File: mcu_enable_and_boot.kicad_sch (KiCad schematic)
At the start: 12 parts, among them SW1 TS_Basic_Small, SW2 TS_Basic_Small

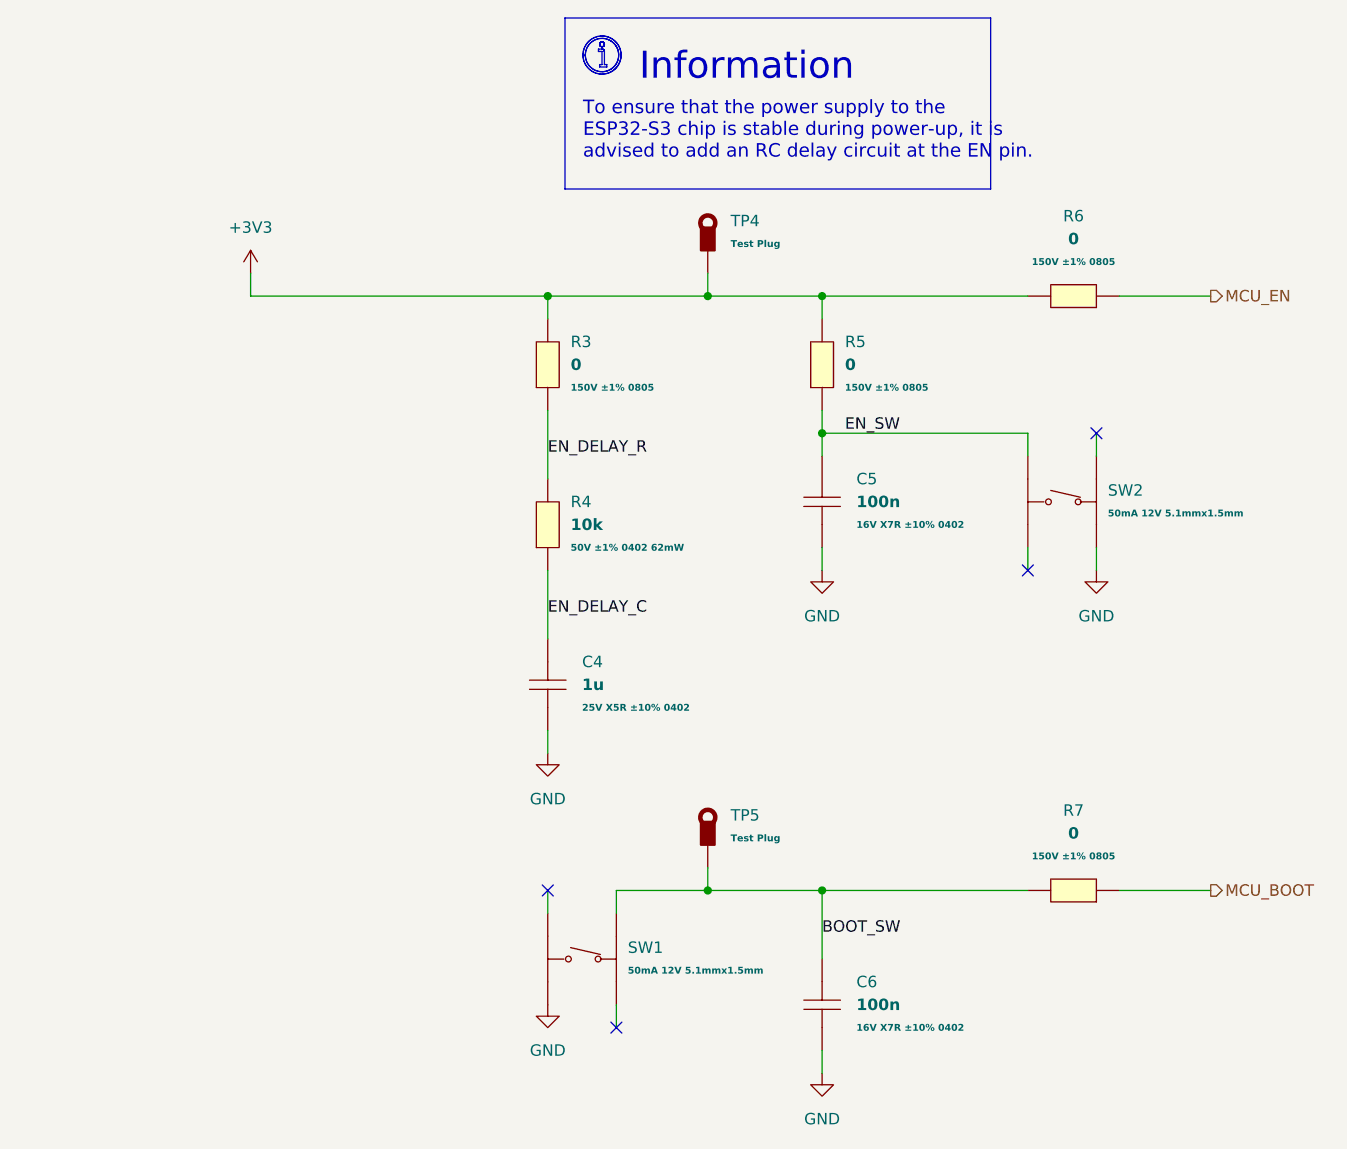
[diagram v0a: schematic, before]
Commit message: Updated library name, updated and verified all footprints
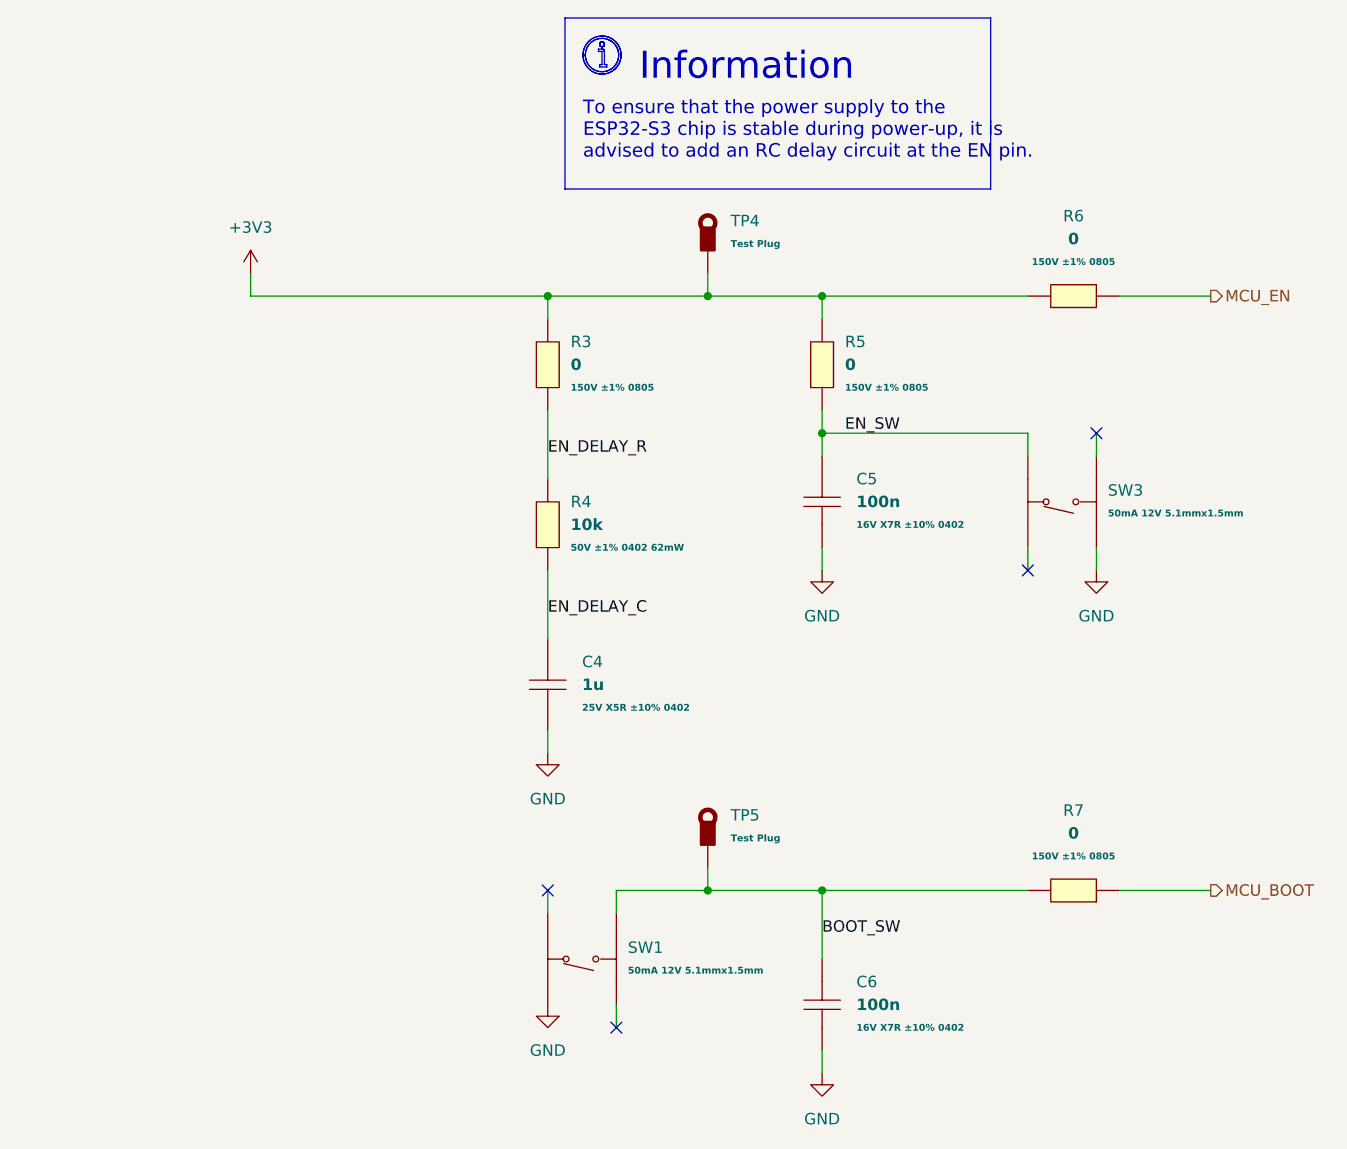
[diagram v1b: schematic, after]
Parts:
- removed SW1, SW2: TS_Basic_Small, EASYEDA2KICAD:SW-SMD_4P-L5.1-W5.1-P3.70-LS6.5-TL-2, symbol EASYEDA2KICAD:TS_Small_Basic
- added SW1, SW3: TS_Basic_Small, LiveAstra:SW-SMD_4P-L5.1-W5.1-P3.70-LS6.5-TL-2, symbol LiveAstra:TACTILE_SWITCH_Small_Basic
- C4: symbol EASYEDA2KICAD:C_1uF_X5R_0402 -> LiveAstra:C_1uF_X5R_0402
- C5, C6: symbol EASYEDA2KICAD:C_100nF_X7R_0402 -> LiveAstra:C_100nF_X7R_0402
- R3, R5, R6, R7: symbol EASYEDA2KICAD:R_0Ohm_0805_125mW -> LiveAstra:R_0Ohm_0805_125mW
- R4: symbol EASYEDA2KICAD:R_10kOhm_0402_62mW -> LiveAstra:R_10kOhm_0402_62mW
- TP4, TP5: symbol EASYEDA2KICAD:TestPoint_Thimble -> LiveAstra:TestPoint_Thimble
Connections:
- net BOOT_SW: now also SW1.4 (D)
- net EN_SW: now also SW3.2 (B)
- net GND: now also SW1.1 (A), SW3.3 (C)
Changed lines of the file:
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@@
 	)
 	(symbol
-		(lib_id "EASYEDA2KICAD:C_100nF_X7R_0402")
+		(lib_id "LiveAstra:C_100nF_X7R_0402")
 		(at 152.4 93.98 90)
 		(unit 1)
@@
 	)
 	(symbol
-		(lib_id "EASYEDA2KICAD:R_0Ohm_0805_125mW")
+		(lib_id "LiveAstra:R_0Ohm_0805_125mW")
 		(at 152.4 78.74 90)
 		(unit 1)
@@
 	)
 	(symbol
-		(lib_id "EASYEDA2KICAD:R_10kOhm_0402_62mW")
+		(lib_id "LiveAstra:R_10kOhm_0402_62mW")
 		(at 121.92 96.52 90)
 		(unit 1)
@@
 	)
 	(symbol
-		(lib_id "EASYEDA2KICAD:R_0Ohm_0805_125mW")
+		(lib_id "LiveAstra:R_0Ohm_0805_125mW")
 		(at 180.34 71.12 180)
 		(unit 1)
@@
 	)
 	(symbol
-		(lib_id "EASYEDA2KICAD:TestPoint_Thimble")
+		(lib_id "LiveAstra:TestPoint_Thimble")
 		(at 139.7 68.58 0)
 		(unit 1)
@@
 	)
 	(symbol
-		(lib_id "EASYEDA2KICAD:TS_Small_Basic")
-		(at 180.34 93.98 270)
-		(unit 1)
-		(exclude_from_sim no)
-		(in_bom yes)
-		(on_board yes)
-		(dnp no)
-		(fields_autoplaced yes)
-		(property "Reference" "SW2"
+		(lib_id "LiveAstra:TACTILE_SWITCH_Small_Basic")
+		(at 177.8 93.98 90)
+		(unit 1)
+		(exclude_from_sim no)
+		(in_bom yes)
+		(on_board yes)
+		(dnp no)
+		(fields_autoplaced yes)
+		(property "Reference" "SW3"
 			(at 184.15 92.7099 90)
 			(effects
@@
 					(size 1.27 1.27)
 				)
-				(justify left)
+				(justify right)
 			)
 		)
 		(property "Value" "TS_Basic_Small"
-			(at 166.37 93.98 0)
-			(effects
-				(font
-					(size 1.27 1.27)
-				)
-				(hide yes)
-			)
-		)
-		(property "Footprint" "EASYEDA2KICAD:SW-SMD_4P-L5.1-W5.1-P3.70-LS6.5-TL-2"
-			(at 158.75 93.98 0)
+			(at 191.77 93.98 0)
+			(effects
+				(font
+					(size 1.27 1.27)
+				)
+				(hide yes)
+			)
+		)
+		(property "Footprint" "LiveAstra:SW-SMD_4P-L5.1-W5.1-P3.70-LS6.5-TL-2"
+			(at 199.39 93.98 0)
 			(effects
 				(font
@@
 		)
 		(property "Datasheet" "https://lcsc.com/product-detail/Tactile-Switches_XKB-Enterprise-TS-1187-B-A-A_C318884.html"
-			(at 162.56 93.98 0)
+			(at 195.58 93.98 0)
 			(effects
 				(font
@@
 		)
 		(property "Description" "50mA 5.1mm 100,000 Times 160gf 12V 5.1mm 1.5mm Round Button Brick nogging SPST SMD Tactile Switches ROHS"
-			(at 170.18 93.98 0)
+			(at 187.96 93.98 0)
 			(effects
 				(font
@@
 		)
 		(property "LCSC Part" "C318884"
-			(at 154.94 93.98 0)
+			(at 203.2 93.98 0)
 			(effects
 				(font
@@
 					(bold yes)
 				)
-				(justify left)
-			)
+				(justify right)
+			)
+		)
+		(pin "2"
+		)
+		(pin "1"
 		)
 		(pin "4"
@@
 		(pin "3"
 		)
-		(pin "2"
-		)
-		(pin "1"
-		)
-		(instances
-			(project "AstraControl"
-				(path "/9a751838-dce8-4d69-8a02-736625ac74e7/0db21d8e-3390-4d67-877f-0e5d98e37848/d7820a84-5a43-4050-a708-637b006ce625"
-					(reference "SW2")
-					(unit 1)
-				)
-			)
-		)
-	)
-	(symbol
-		(lib_id "EASYEDA2KICAD:R_0Ohm_0805_125mW")
+		(instances
+			(project ""
+				(path "/9a751838-dce8-4d69-8a02-736625ac74e7/0db21d8e-3390-4d67-877f-0e5d98e37848/d7820a84-5a43-4050-a708-637b006ce625"
+					(reference "SW3")
+					(unit 1)
+				)
+			)
+		)
+	)
+	(symbol
+		(lib_id "LiveAstra:R_0Ohm_0805_125mW")
 		(at 121.92 78.74 90)
 		(unit 1)
@@
 	)
 	(symbol
-		(lib_id "EASYEDA2KICAD:R_0Ohm_0805_125mW")
+		(lib_id "LiveAstra:R_0Ohm_0805_125mW")
 		(at 180.34 137.16 180)
 		(unit 1)
@@
 	)
 	(symbol
-		(lib_id "EASYEDA2KICAD:C_100nF_X7R_0402")
+		(lib_id "LiveAstra:TACTILE_SWITCH_Small_Basic")
+		(at 124.46 144.78 90)
+		(unit 1)
+		(exclude_from_sim no)
+		(in_bom yes)
+		(on_board yes)
+		(dnp no)
+		(fields_autoplaced yes)
+		(property "Reference" "SW1"
+			(at 130.81 143.5099 90)
+			(effects
+				(font
+					(size 1.27 1.27)
+				)
+				(justify right)
+			)
+		)
+		(property "Value" "TS_Basic_Small"
+			(at 138.43 144.78 0)
+			(effects
+				(font
+					(size 1.27 1.27)
+				)
+				(hide yes)
+			)
+		)
+		(property "Footprint" "LiveAstra:SW-SMD_4P-L5.1-W5.1-P3.70-LS6.5-TL-2"
+			(at 146.05 144.78 0)
+			(effects
+				(font
+					(size 1.27 1.27)
+				)
+				(hide yes)
+			)
+		)
+		(property "Datasheet" "https://lcsc.com/product-detail/Tactile-Switches_XKB-Enterprise-TS-1187-B-A-A_C318884.html"
+			(at 142.24 144.78 0)
+			(effects
+				(font
+					(size 1.27 1.27)
+				)
+				(hide yes)
+			)
+		)
+		(property "Description" "50mA 5.1mm 100,000 Times 160gf 12V 5.1mm 1.5mm Round Button Brick nogging SPST SMD Tactile Switches ROHS"
+			(at 134.62 144.78 0)
+			(effects
+				(font
+					(size 1.27 1.27)
+				)
+				(hide yes)
+			)
+		)
+		(property "LCSC Part" "C318884"
+			(at 149.86 144.78 0)
+			(effects
+				(font
+					(size 1.27 1.27)
+				)
+				(hide yes)
+			)
+		)
+		(property "Extra Values" "50mA 12V 5.1mmx1.5mm"
+			(at 130.81 146.0499 90)
+			(effects
+				(font
+					(size 0.762 0.762)
+					(bold yes)
+				)
+				(justify right)
+			)
+		)
+		(pin "2"
+		)
+		(pin "1"
+		)
+		(pin "4"
+		)
+		(pin "3"
+		)
+		(instances
+			(project "AstraControl"
+				(path "/9a751838-dce8-4d69-8a02-736625ac74e7/0db21d8e-3390-4d67-877f-0e5d98e37848/d7820a84-5a43-4050-a708-637b006ce625"
+					(reference "SW1")
+					(unit 1)
+				)
+			)
+		)
+	)
+	(symbol
+		(lib_id "LiveAstra:C_100nF_X7R_0402")
 		(at 152.4 149.86 270)
 		(unit 1)
@@
 	)
 	(symbol
-		(lib_id "EASYEDA2KICAD:C_1uF_X5R_0402")
+		(lib_id "LiveAstra:C_1uF_X5R_0402")
 		(at 121.92 114.3 90)
 		(unit 1)
@@
 	)
 	(symbol
-		(lib_id "EASYEDA2KICAD:TS_Small_Basic")
-		(at 127 144.78 270)
-		(unit 1)
-		(exclude_from_sim no)
-		(in_bom yes)
-		(on_board yes)
-		(dnp no)
-		(fields_autoplaced yes)
-		(property "Reference" "SW1"
-			(at 130.81 143.5099 90)
-			(effects
-				(font
-					(size 1.27 1.27)
-				)
-				(justify left)
-			)
-		)
-		(property "Value" "TS_Basic_Small"
-			(at 113.03 144.78 0)
-			(effects
-				(font
-					(size 1.27 1.27)
-				)
-				(hide yes)
-			)
-		)
-		(property "Footprint" "EASYEDA2KICAD:SW-SMD_4P-L5.1-W5.1-P3.70-LS6.5-TL-2"
-			(at 105.41 144.78 0)
-			(effects
-				(font
-					(size 1.27 1.27)
-				)
-				(hide yes)
-			)
-		)
-		(property "Datasheet" "https://lcsc.com/product-detail/Tactile-Switches_XKB-Enterprise-TS-1187-B-A-A_C318884.html"
-			(at 109.22 144.78 0)
-			(effects
-				(font
-					(size 1.27 1.27)
-				)
-				(hide yes)
-			)
-		)
-		(property "Description" "50mA 5.1mm 100,000 Times 160gf 12V 5.1mm 1.5mm Round Button Brick nogging SPST SMD Tactile Switches ROHS"
-			(at 116.84 144.78 0)
-			(effects
-				(font
-					(size 1.27 1.27)
-				)
-				(hide yes)
-			)
-		)
-		(property "LCSC Part" "C318884"
-			(at 101.6 144.78 0)
-			(effects
-				(font
-					(size 1.27 1.27)
-				)
-				(hide yes)
-			)
-		)
-		(property "Extra Values" "50mA 12V 5.1mmx1.5mm"
-			(at 130.81 146.0499 90)
-			(effects
-				(font
-					(size 0.762 0.762)
-					(bold yes)
-				)
-				(justify left)
-			)
-		)
-		(pin "4"
-		)
-		(pin "3"
-		)
-		(pin "2"
-		)
-		(pin "1"
-		)
-		(instances
-			(project "AstraControl"
-				(path "/9a751838-dce8-4d69-8a02-736625ac74e7/0db21d8e-3390-4d67-877f-0e5d98e37848/d7820a84-5a43-4050-a708-637b006ce625"
-					(reference "SW1")
-					(unit 1)
-				)
-			)
-		)
-	)
-	(symbol
-		(lib_id "EASYEDA2KICAD:TestPoint_Thimble")
+		(lib_id "LiveAstra:TestPoint_Thimble")
 		(at 139.7 134.62 0)
 		(unit 1)

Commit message: Finished layout no drc or erc errors
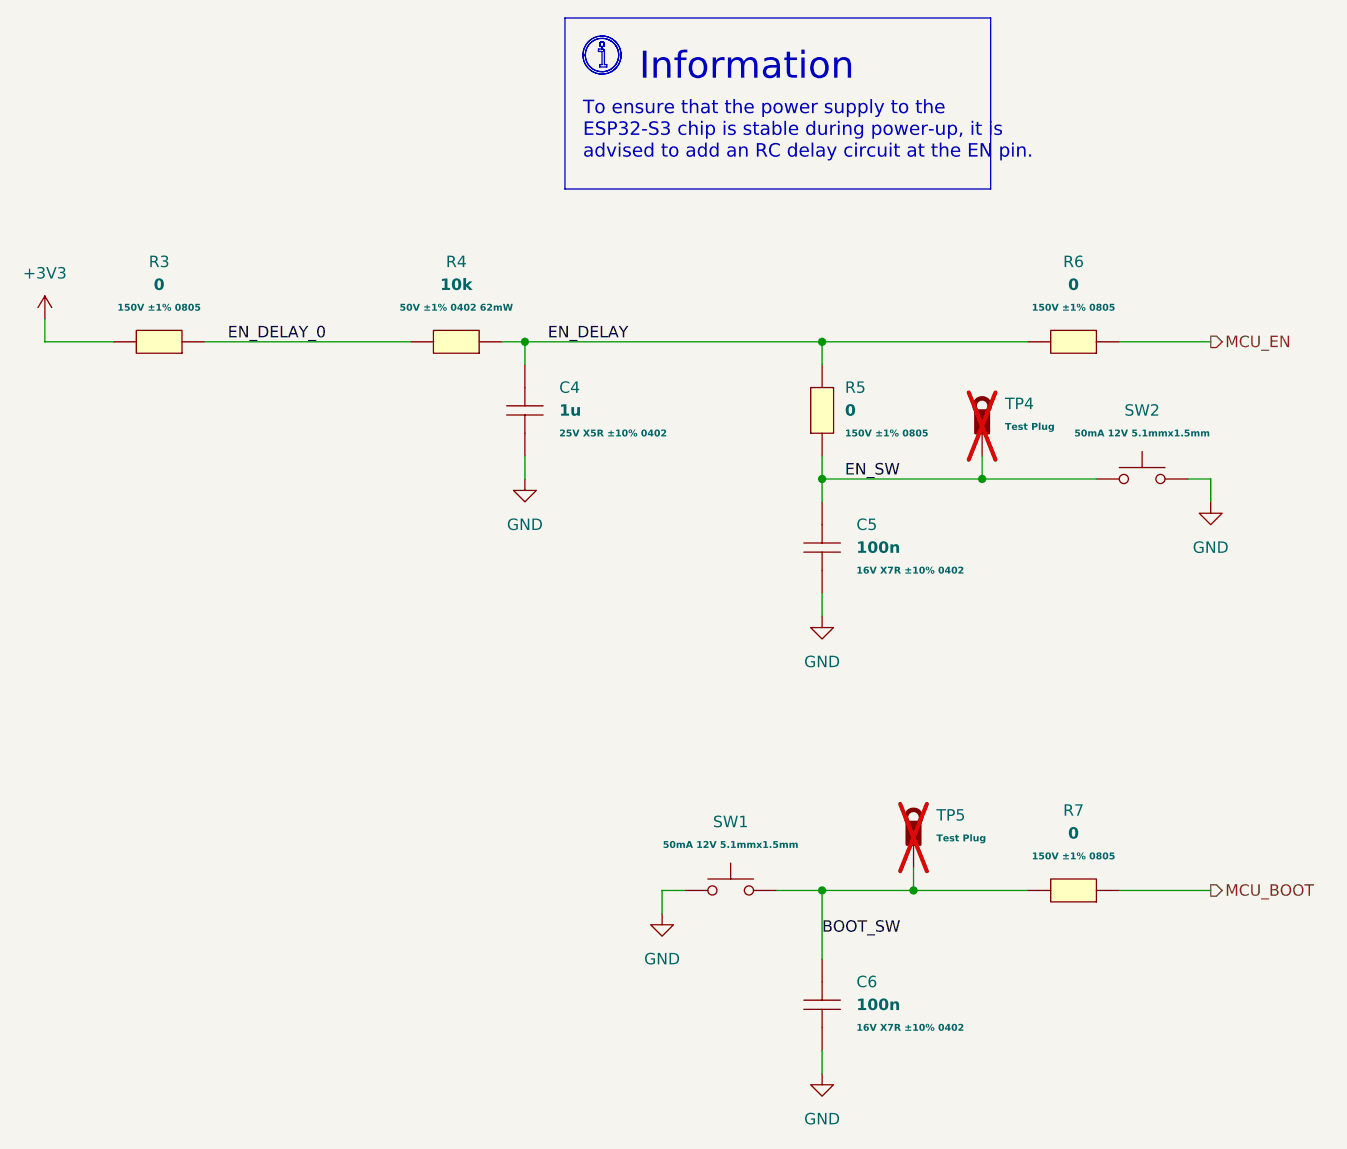
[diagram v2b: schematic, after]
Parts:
- removed SW3: TS_Basic_Small, LiveAstra:SW-SMD_4P-L5.1-W5.1-P3.70-LS6.5-TL-2, symbol LiveAstra:TACTILE_SWITCH_Small_Basic
- added SW2: TS_Basic_Small, LiveAstra:TACTILE_SWITCH-SMD_4P-L5.1-W5.1-P3.70-LS6.5-TL-2, symbol LiveAstra:TACTILE_SWITCH_Small_Basic
- C4, C5, C6: footprint Capacitor_SMD:C_0402_1005Metric -> LiveAstra:C_0402_1005Metric
- R3, R5, R6, R7: footprint Resistor_SMD:R_0805_2012Metric_Pad1.20x1.40mm_HandSolder -> LiveAstra:R_0805_2012Metric_Pad1.20x1.40mm_HandSolder
- R4: footprint Resistor_SMD:R_0402_1005Metric -> LiveAstra:R_0402_1005Metric
- SW1: footprint LiveAstra:SW-SMD_4P-L5.1-W5.1-P3.70-LS6.5-TL-2 -> LiveAstra:TACTILE_SWITCH-SMD_4P-L5.1-W5.1-P3.70-LS6.5-TL-2
- TP4, TP5: footprint TestPoint:TestPoint_Loop_D3.50mm_Drill0.9mm_Beaded -> LiveAstra:TestPoint_Loop_D3.50mm_Drill0.9mm_Beaded; now not fitted; now left out of the parts list
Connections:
- net +3V3: no longer R5.2, R6.2, TP4.1
- net BOOT_SW: now also SW1.2; no longer SW1.4 (D)
- net EN_SW: now also TP4.1, SW2.1
- net GND: now also C4.2, SW2.2; no longer C4.1
- net EN_DELAY_C renamed EN_DELAY
- net EN_DELAY: now also C4.1, R5.2, R6.2; no longer C4.2
- net EN_DELAY_R renamed EN_DELAY_0
- no-connect marks 4 -> 0
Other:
- moved on the sheet: C4, C5, R3, R4, R5, R6
